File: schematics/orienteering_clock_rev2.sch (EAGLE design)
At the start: 60 parts, among them IC1 TPIC6B595N, IC2 TPIC6B595N, J2 ICSP, Q1 IRFU9024V, Q2 IRFU9024V, Q3 IRFU9024V, Q4 IRFU9024V, Q5 IRFU9024V, Q6 IRFU9024V, T1 BC547, Y1 16MHz

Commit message: schematics: finishing touches
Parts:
- JP1: device SparkFun-Connectors:M03JST-PTH -> SparkFun-Connectors:M03POLAR
- LM7805: device v-reg:78XXS -> MINE:78XXS
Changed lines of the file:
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@@
 <classes>
 <class number="0" name="default" width="0.3048" drill="0.3048">
-<clearance class="0" value="0.254"/>
+<clearance class="0" value="0.3048"/>
 </class>
 <class number="1" name="power" width="0.8128" drill="0.6096">
@@
 </class>
 <class number="3" name="SPI" width="0.4064" drill="0">
-<clearance class="3" value="0.254"/>
+<clearance class="3" value="0.3048"/>
 </class>
 </classes>
@@
 <part name="GND4" library="supply1" deviceset="GND" device=""/>
 <part name="JP3" library="SparkFun-Connectors" deviceset="M02" device="LOCK" value="BUZZER"/>
-<part name="JP1" library="SparkFun-Connectors" deviceset="M03" device="JST-PTH" value="DC_IN"/>
+<part name="JP1" library="SparkFun-Connectors" deviceset="M03" device="POLAR" value="DC_IN"/>
 <part name="JP5" library="SparkFun-Connectors" deviceset="M08" device="" value="LED_CATHODE"/>
 <part name="JP6" library="SparkFun-Connectors" deviceset="M04" device="PTH" value="LED_ANODE"/>
@@
 <part name="JP2" library="SparkFun-Connectors" deviceset="M03" device="LOCK" value="POWER_OUT"/>
 <part name="SJ1" library="SparkFun-Passives" deviceset="JUMPER-PAD-2-NC_BY_TRACE" device="" value="SHDN_PULLUP"/>
-<part name="LM7805" library="v-reg" deviceset="78XXS" device=""/>
+<part name="LM7805" library="MINE" deviceset="78XXS" device=""/>
 <part name="C6" library="SparkFun-Passives" deviceset="CAP_POL" device="PTH1" value="470uF"/>
 <part name="C7" library="SparkFun-Passives" deviceset="CAP_POL" device="PTH1" value="470uF"/>
@@
 </segment>
 </net>
-<net name="AREF" class="0">
+<net name="AREF" class="3">
 <segment>
 <wire x1="180.34" y1="40.64" x2="175.26" y2="40.64" width="0.1524" layer="91"/>
@@
 </segment>
 </net>
-<net name="BUZZ_-" class="0">
+<net name="BUZZ_-" class="3">
 <segment>
 <label x="76.2" y="73.66" size="1.778" layer="95" rot="MR270"/>

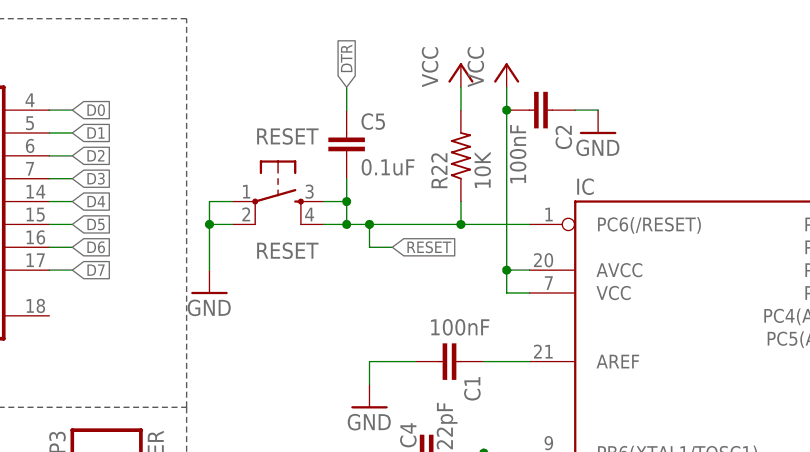
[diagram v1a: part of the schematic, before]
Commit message: schematics: fix errors on silkscreen
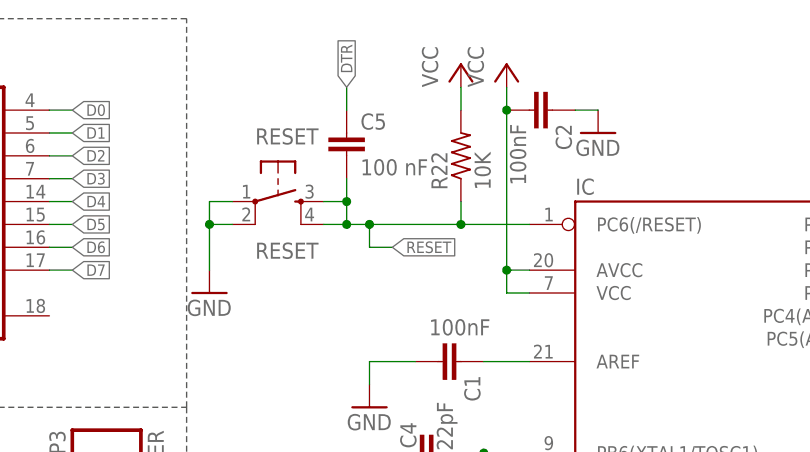
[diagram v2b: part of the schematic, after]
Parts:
- C5: value 0.1uF -> 100 nF
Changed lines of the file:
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@@
 <grid distance="0.1" unitdist="inch" unit="inch" style="lines" multiple="1" display="no" altdistance="0.01" altunitdist="inch" altunit="inch"/>
 <layers>
-<layer number="1" name="Top" color="4" fill="1" visible="yes" active="no"/>
-<layer number="16" name="Bottom" color="1" fill="1" visible="yes" active="no"/>
-<layer number="17" name="Pads" color="2" fill="1" visible="yes" active="no"/>
-<layer number="18" name="Vias" color="2" fill="1" visible="yes" active="no"/>
-<layer number="19" name="Unrouted" color="6" fill="1" visible="yes" active="no"/>
-<layer number="20" name="Dimension" color="15" fill="1" visible="yes" active="no"/>
-<layer number="21" name="tPlace" color="7" fill="1" visible="yes" active="no"/>
-<layer number="22" name="bPlace" color="7" fill="1" visible="yes" active="no"/>
-<layer number="23" name="tOrigins" color="15" fill="1" visible="yes" active="no"/>
-<layer number="24" name="bOrigins" color="15" fill="1" visible="yes" active="no"/>
-<layer number="25" name="tNames" color="7" fill="1" visible="yes" active="no"/>
-<layer number="26" name="bNames" color="7" fill="1" visible="yes" active="no"/>
-<layer number="27" name="tValues" color="7" fill="1" visible="yes" active="no"/>
-<layer number="28" name="bValues" color="7" fill="1" visible="yes" active="no"/>
+<layer number="1" name="Top" color="4" fill="1" visible="no" active="no"/>
+<layer number="16" name="Bottom" color="1" fill="1" visible="no" active="no"/>
+<layer number="17" name="Pads" color="2" fill="1" visible="no" active="no"/>
+<layer number="18" name="Vias" color="2" fill="1" visible="no" active="no"/>
+<layer number="19" name="Unrouted" color="6" fill="1" visible="no" active="no"/>
+<layer number="20" name="Dimension" color="15" fill="1" visible="no" active="no"/>
+<layer number="21" name="tPlace" color="7" fill="1" visible="no" active="no"/>
+<layer number="22" name="bPlace" color="7" fill="1" visible="no" active="no"/>
+<layer number="23" name="tOrigins" color="15" fill="1" visible="no" active="no"/>
+<layer number="24" name="bOrigins" color="15" fill="1" visible="no" active="no"/>
+<layer number="25" name="tNames" color="7" fill="1" visible="no" active="no"/>
+<layer number="26" name="bNames" color="7" fill="1" visible="no" active="no"/>
+<layer number="27" name="tValues" color="7" fill="1" visible="no" active="no"/>
+<layer number="28" name="bValues" color="7" fill="1" visible="no" active="no"/>
 <layer number="29" name="tStop" color="7" fill="3" visible="no" active="no"/>
 <layer number="30" name="bStop" color="7" fill="6" visible="no" active="no"/>
@@
 <layer number="35" name="tGlue" color="7" fill="4" visible="no" active="no"/>
 <layer number="36" name="bGlue" color="7" fill="5" visible="no" active="no"/>
-<layer number="37" name="tTest" color="7" fill="1" visible="yes" active="no"/>
-<layer number="38" name="bTest" color="7" fill="1" visible="yes" active="no"/>
+<layer number="37" name="tTest" color="7" fill="1" visible="no" active="no"/>
+<layer number="38" name="bTest" color="7" fill="1" visible="no" active="no"/>
 <layer number="39" name="tKeepout" color="4" fill="11" visible="no" active="no"/>
 <layer number="40" name="bKeepout" color="1" fill="11" visible="no" active="no"/>
@@
 <layer number="44" name="Drills" color="7" fill="1" visible="no" active="no"/>
 <layer number="45" name="Holes" color="7" fill="1" visible="no" active="no"/>
-<layer number="46" name="Milling" color="3" fill="1" visible="yes" active="no"/>
-<layer number="47" name="Measures" color="7" fill="1" visible="yes" active="no"/>
-<layer number="48" name="Document" color="7" fill="1" visible="yes" active="no"/>
-<layer number="49" name="Reference" color="7" fill="1" visible="yes" active="no"/>
-<layer number="50" name="dxf" color="7" fill="1" visible="yes" active="no"/>
-<layer number="51" name="tDocu" color="7" fill="1" visible="yes" active="no"/>
-<layer number="52" name="bDocu" color="7" fill="1" visible="yes" active="no"/>
-<layer number="53" name="tGND_GNDA" color="7" fill="1" visible="yes" active="no"/>
-<layer number="54" name="bGND_GNDA" color="7" fill="1" visible="yes" active="no"/>
-<layer number="56" name="wert" color="7" fill="1" visible="yes" active="no"/>
-<layer number="57" name="tCAD" color="7" fill="1" visible="yes" active="no"/>
+<layer number="46" name="Milling" color="3" fill="1" visible="no" active="no"/>
+<layer number="47" name="Measures" color="7" fill="1" visible="no" active="no"/>
+<layer number="48" name="Document" color="7" fill="1" visible="no" active="no"/>
+<layer number="49" name="Reference" color="7" fill="1" visible="no" active="no"/>
+<layer number="50" name="dxf" color="7" fill="1" visible="no" active="no"/>
+<layer number="51" name="tDocu" color="7" fill="1" visible="no" active="no"/>
+<layer number="52" name="bDocu" color="7" fill="1" visible="no" active="no"/>
+<layer number="53" name="tGND_GNDA" color="7" fill="1" visible="no" active="no"/>
+<layer number="54" name="bGND_GNDA" color="7" fill="1" visible="no" active="no"/>
+<layer number="56" name="wert" color="7" fill="1" visible="no" active="no"/>
+<layer number="57" name="tCAD" color="7" fill="1" visible="no" active="no"/>
 <layer number="90" name="Modules" color="5" fill="1" visible="yes" active="yes"/>
 <layer number="91" name="Nets" color="2" fill="1" visible="yes" active="yes"/>
@@
 <part name="GND7" library="SparkFun" deviceset="GND" device=""/>
 <part name="GND8" library="SparkFun" deviceset="GND" device=""/>
-<part name="C5" library="SparkFun" deviceset="CAP" device="PTH" value="0.1uF"/>
+<part name="C5" library="SparkFun" deviceset="CAP" device="PTH" value="100 nF"/>
 <part name="IC" library="SparkFun-DigitalIC" deviceset="ATMEGA328P_PDIP" device="" value="ATMEGA328"/>
 <part name="IOH" library="SparkFun-Connectors" deviceset="M10" device="LOCK" value="M10LOCK"/>

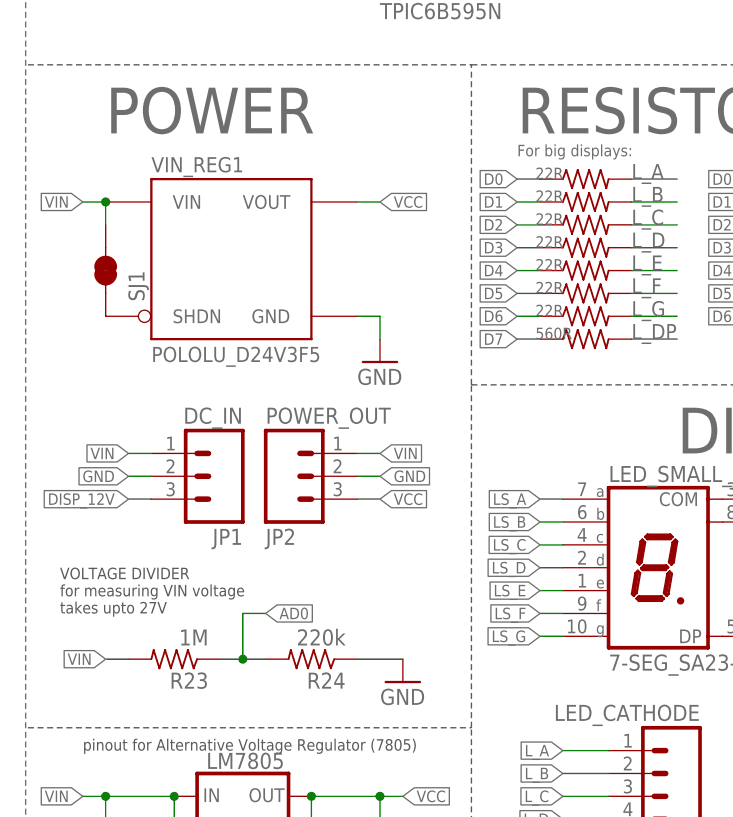
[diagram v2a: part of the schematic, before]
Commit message: schematics: updated voltage sense, resistor values for new display
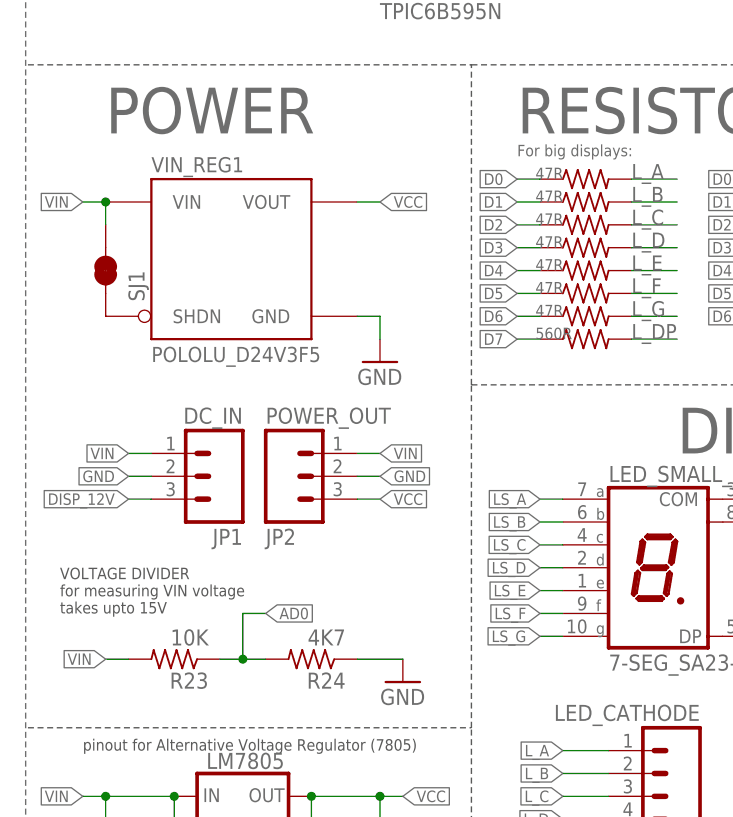
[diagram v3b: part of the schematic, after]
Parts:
- R10, R11, R12, R13, R7, R8, R9: value 22R -> 47R
- R23: value 1M -> 10K
- R24: value 220k -> 4K7
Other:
- note added: "VOLTAGE DIVIDER for measuring VIN voltage takes upto 15V"
- note removed: "VOLTAGE DIVIDER for measuring VIN voltage takes upto 27V"
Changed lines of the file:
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@@
 <part name="R1" library="resistor" deviceset="R-US_" device="0207/5V" value="22k"/>
 <part name="IC1" library="NumericDisplay" deviceset="TPIC6B595" device="N"/>
-<part name="R8" library="resistor" deviceset="R-US_" device="0207/10" value="22R"/>
-<part name="R7" library="resistor" deviceset="R-US_" device="0207/10" value="22R"/>
-<part name="R9" library="resistor" deviceset="R-US_" device="0207/10" value="22R"/>
-<part name="R10" library="resistor" deviceset="R-US_" device="0207/10" value="22R"/>
-<part name="R11" library="resistor" deviceset="R-US_" device="0207/10" value="22R"/>
-<part name="R12" library="resistor" deviceset="R-US_" device="0207/10" value="22R"/>
-<part name="R13" library="resistor" deviceset="R-US_" device="0207/10" value="22R"/>
+<part name="R8" library="resistor" deviceset="R-US_" device="0207/10" value="47R"/>
+<part name="R7" library="resistor" deviceset="R-US_" device="0207/10" value="47R"/>
+<part name="R9" library="resistor" deviceset="R-US_" device="0207/10" value="47R"/>
+<part name="R10" library="resistor" deviceset="R-US_" device="0207/10" value="47R"/>
+<part name="R11" library="resistor" deviceset="R-US_" device="0207/10" value="47R"/>
+<part name="R12" library="resistor" deviceset="R-US_" device="0207/10" value="47R"/>
+<part name="R13" library="resistor" deviceset="R-US_" device="0207/10" value="47R"/>
 <part name="IC2" library="NumericDisplay" deviceset="TPIC6B595" device="N"/>
 <part name="P+1" library="supply1" deviceset="+12V" device="" value="DISP_12V"/>
@@
 <part name="R21" library="resistor" deviceset="R-US_" device="0207/10" value="560R"/>
 <part name="JP7" library="SparkFun-Connectors" deviceset="FTDI_DEVICE" device=""/>
-<part name="R23" library="resistor" deviceset="R-US_" device="0207/10" value="1M"/>
-<part name="R24" library="resistor" deviceset="R-US_" device="0207/10" value="220k"/>
+<part name="R23" library="resistor" deviceset="R-US_" device="0207/10" value="10K"/>
+<part name="R24" library="resistor" deviceset="R-US_" device="0207/10" value="4K7"/>
 <part name="GND2" library="SparkFun" deviceset="GND" device=""/>
 <part name="JP2" library="SparkFun-Connectors" deviceset="M03" device="LOCK" value="POWER_OUT"/>
@@
 <text x="-43.18" y="22.86" size="1.27" layer="97">VOLTAGE DIVIDER
 for measuring VIN voltage
-takes upto 27V</text>
+takes upto 15V</text>
 <wire x1="-46.736" y1="-15.24" x2="2.54" y2="-15.24" width="0.1524" layer="97" style="shortdash"/>
 <text x="54.61" y="49.022" size="1.27" layer="97">Set IO8 to HIGH to enable BUZZER</text>
